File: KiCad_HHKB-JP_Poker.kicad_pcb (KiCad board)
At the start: 2 copper layers, 285 x 95.1 mm, 155 parts, among them SW1 SW_Push, U1 ATmega32U4-MU, U2 PRTR5V0U2X, Y1 16MHz

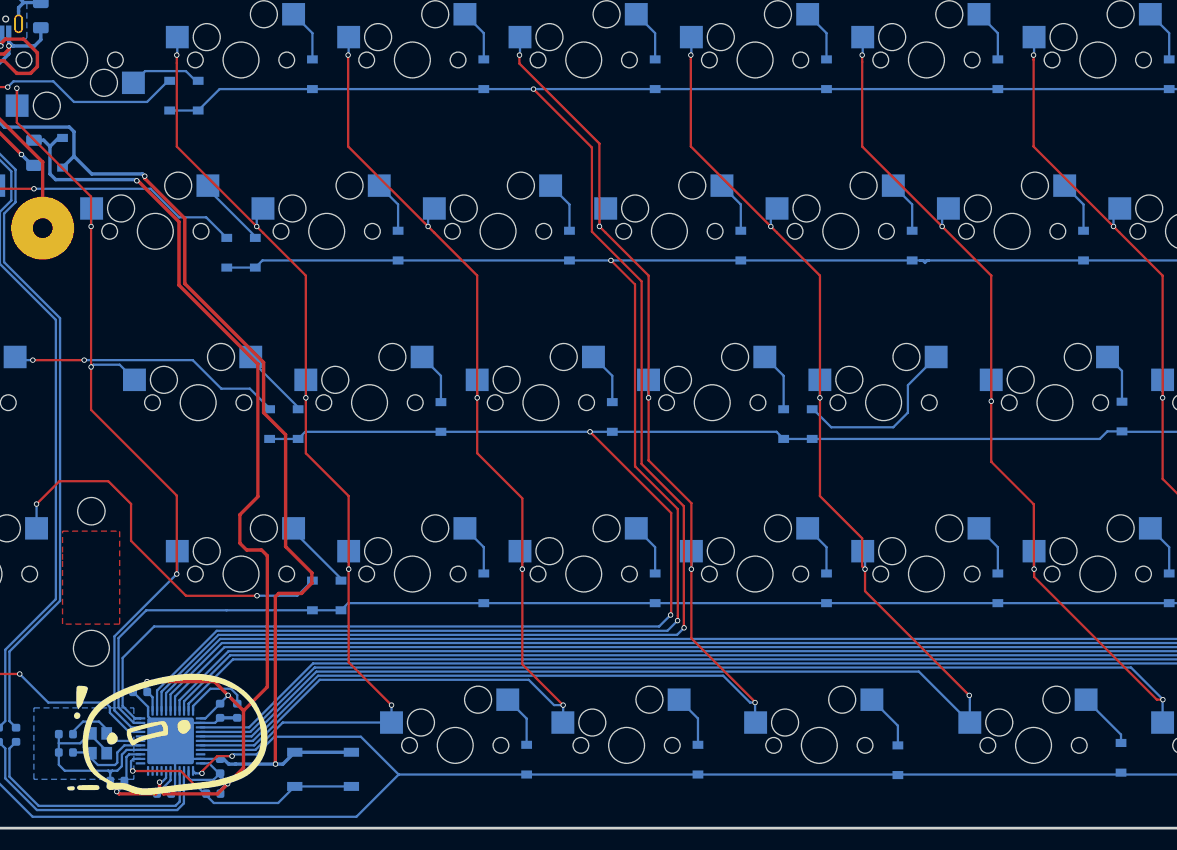
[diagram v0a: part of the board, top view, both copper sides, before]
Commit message: 電源配線を穴を避けて配線しなおした
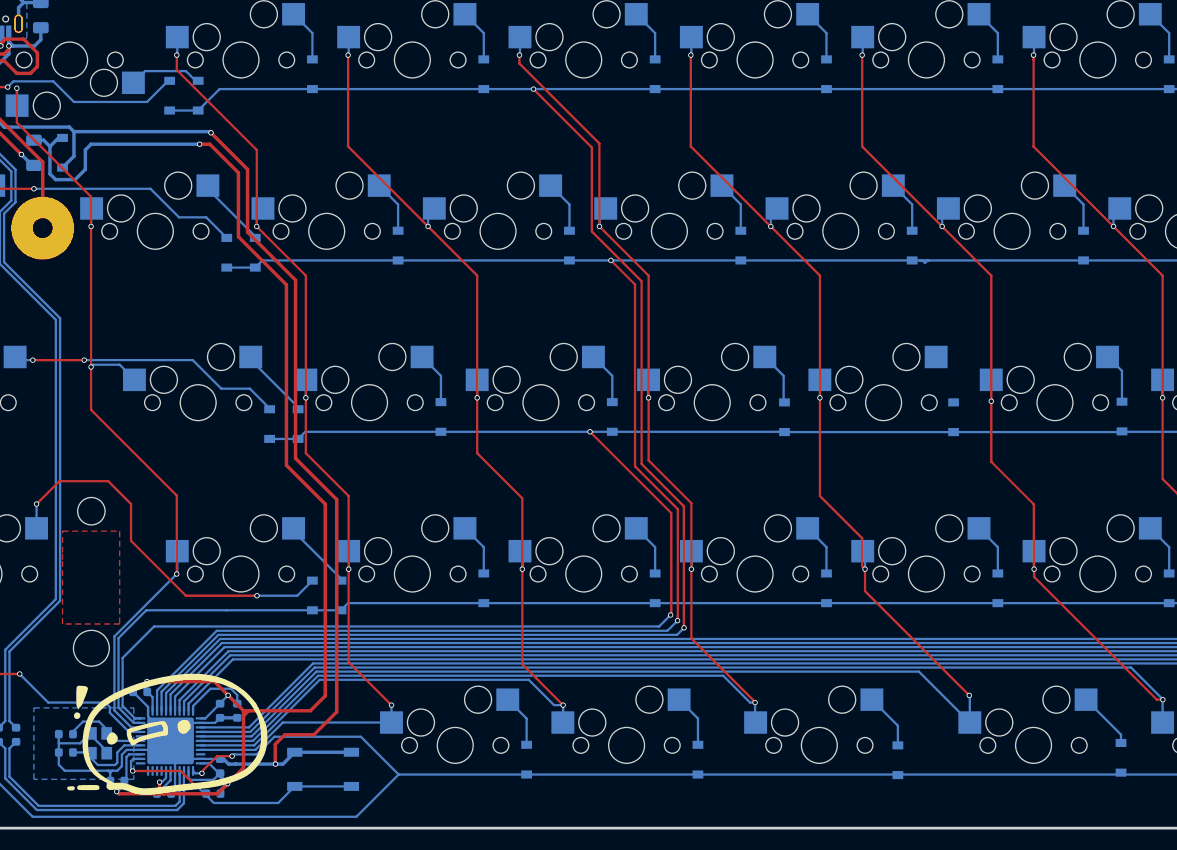
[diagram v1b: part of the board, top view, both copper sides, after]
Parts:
- moved D28 15.7 mm to (251.5, 221.5)
- moved D23 0.77 mm to (232.7, 221.5)
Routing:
- net +5V: track 146.1 -> 166.4 mm
- net Net-(D28-Pad2): track 19.6 -> 0.00 mm
- net GND: track 202.3 -> 213.2 mm
- net ROW2: track 306.3 -> 305.6 mm
- net Net-(D23-Pad2): track 6.68 -> 5.96 mm

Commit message: DRCチェック（未配線を修正）
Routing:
- net Net-(D28-Pad2): track 0.00 -> 5.85 mm
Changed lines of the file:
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@@
   (segment (start 246.85625 197.83425) (end 244.76075 195.73875) (width 0.254) (layer "B.Cu") (net 33))
   (segment (start 246.85625 200.75625) (end 246.85625 197.83425) (width 0.254) (layer "B.Cu") (net 33))
+  (segment (start 251.46 216.7255) (end 251.46 219.838) (width 0.254) (layer "B.Cu") (net 34))
+  (segment (start 249.52325 214.78875) (end 251.46 216.7255) (width 0.254) (layer "B.Cu") (net 34))
   (segment (start 256.38125 238.85625) (end 256.38125 235.93425) (width 0.254) (layer "B.Cu") (net 35))
   (segment (start 256.38125 235.93425) (end 254.28575 233.83875) (width 0.254) (layer "B.Cu") (net 35))
